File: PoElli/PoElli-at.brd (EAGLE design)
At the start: 85 x 56 mm, 146 parts, among them J3 M022.54MM, J4 M022.54MM, Q1 SI1307DL, Q2 FDV301N, Q3 FDMC2674, Q4 IRFL4310, SW1 A6H2101, T1 Coilcraft 230NL, T2 FLYBACK750311689, U2 NCP1117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

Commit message: routing draft v0.2, planes & routes in, optimization to be done..
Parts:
- moved C18 37.4 mm to (39.9, 47.0)
- moved C17 36.2 mm to (39.9, 48.0)
- moved TP8 35.5 mm to (2.00, 42.5)
- moved C43 27.6 mm to (37.4, 58.6)
- moved R14 25.1 mm to (22.9, 50.5)
- moved C4 24.4 mm to (12.2, 33.3), turned to 180 degrees
- moved C5 23.6 mm to (11.0, 34.7), turned to 270 degrees
- moved C44 23.3 mm to (37.4, 56.3)
- moved C6 21.1 mm to (10.9, 37.9), turned to 90 degrees
- moved D5 16.3 mm to (33.8, 50.3), turned to 90 degrees
- moved C45 15.7 mm to (37.4, 51.7)
- moved C46 15.0 mm to (37.4, 54.0)
- moved D18 14.0 mm to (36.7, 23.8), turned to 180 degrees
- moved R24 13.5 mm to (47.7, 35.6), turned to 270 degrees
- moved TP7 12.7 mm to (30.7, 40.5)
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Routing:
- net N$9: track 0.00 -> 82.3 mm, vias 0 -> 5
- net 5V: track 0.00 -> 70.9 mm, vias 0 -> 12
- net +3V3: track 0.00 -> 67.3 mm, vias 0 -> 8
- net N$11: track 0.00 -> 66.1 mm, vias 0 -> 2
- net N$12: track 0.00 -> 65.8 mm, vias 0 -> 2
- net N$13: track 0.00 -> 62.7 mm, vias 0 -> 2
- net N$14: track 0.00 -> 60.7 mm, vias 0 -> 2
- net ETH_SCK: track 0.00 -> 56.6 mm, vias 0 -> 2
- net ETH_MUX: track 0.00 -> 52.9 mm, vias 0 -> 4
- net POE_B+: track 0.00 -> 52.9 mm
- net N$21: track 0.00 -> 52.1 mm
- net SS2: track 0.00 -> 49.1 mm, vias 0 -> 2
- net ETH_MISO: track 0.00 -> 44.7 mm, vias 0 -> 2
- net ETH_MOSI: track 0.00 -> 42.4 mm, vias 0 -> 1
- net U4_INTVCC: track 0.00 -> 40.8 mm, vias 0 -> 4
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- added copper zone on layer 15, net +3V3
- added copper zone on layer 15, net 5V
- added copper zone on layer 15, net ENC-3V3
- added copper zone on layer 1, net GNDA
- added copper zone on layer 2, net GNDA
- added copper zone on layer 1, net RTN
- added copper zone on layer 2, net RTN
- added copper zone on layer 15, net VDD

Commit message: gnd vias, planes etc
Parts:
- moved U$2 95.4 mm to (94.7, 11.7)
- moved C41 2.75 mm to (35.3, 21.0)
- moved FB4 1.63 mm to (38.7, 18.1), turned to 90 degrees
- moved C25 1.56 mm to (63.6, 27.5), turned to 180 degrees
- moved R29 0.80 mm to (44.0, 13.2)
- moved R19 0.30 mm to (67.1, 26.8)
- moved C1 0.28 mm to (18.5, 34.2)
- moved D3 0.22 mm to (51.4, 37.9)
- moved R23 0.14 mm to (40.9, 14.4)
- moved R32 0.10 mm to (51.0, 35.5)
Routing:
- net N$76: track 13.3 -> 11.3 mm
- net POE_A-: track 30.6 -> 29.0 mm
- net ETH_MOSI: track 42.4 -> 43.6 mm
- net SS2: track 49.1 -> 50.2 mm
- net N$6: track 30.1 -> 31.1 mm
- net VSS: track 25.7 -> 26.6 mm
- net N$51: track 4.71 -> 5.53 mm
- net N$5: track 14.1 -> 13.3 mm
- net N$19: track 3.78 -> 4.57 mm
- net GNDA: vias 48 -> 139
- added copper zone on layer 16, net GNDA
- added copper zone on layer 16, net RTN

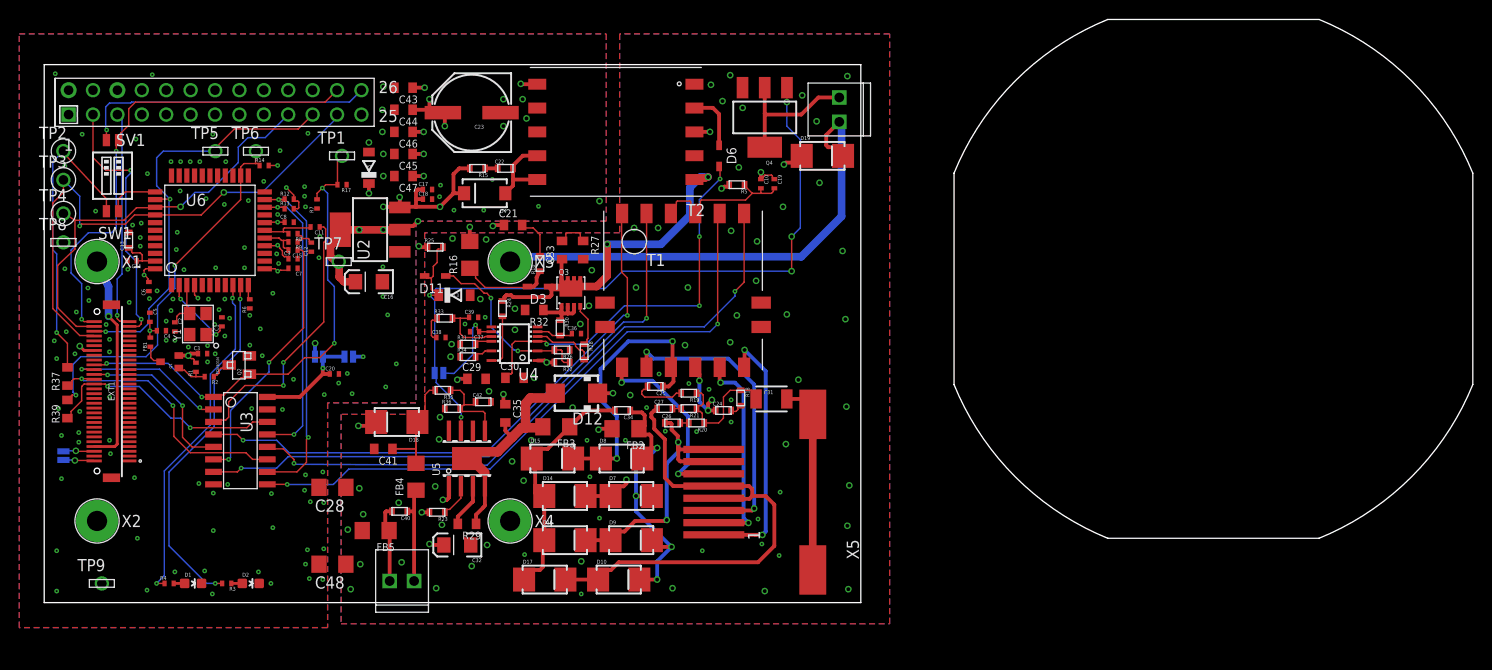
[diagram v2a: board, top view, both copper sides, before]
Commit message: smallest via drill to 0.25mm (was 0.2), + small improvments
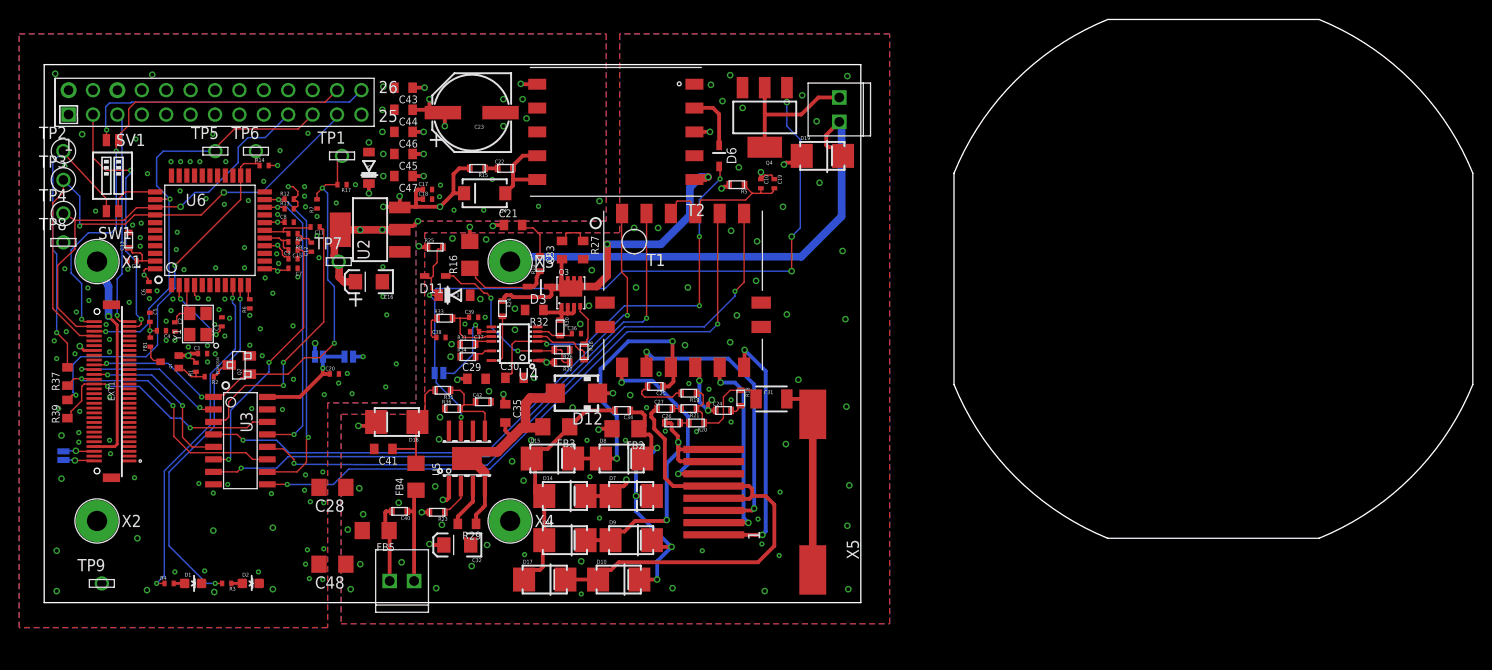
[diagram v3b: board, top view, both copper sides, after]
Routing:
- net +3V3: track 67.1 -> 66.6 mm
- net GNDA: vias 139 -> 145
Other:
- board text added: "+"

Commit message: review changes applied
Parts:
- removed U$2: (no value), ELL-i-Boards:DIN49073-1:2010-02-OUTLINE
- added C49, C50: 10nF, ELL-i-Passives:C0402
- added U$3: (no value), hapines:EH-LOGO
- C21: value 100nF -> 100nF 100V
- moved C19 21.6 mm to (54.7, 45.0), turned to 0 degrees
- moved R5 20.9 mm to (51.4, 45.8)
- moved C10 20.0 mm to (54.7, 46.5), turned to 0 degrees
- moved R10 6.57 mm to (46.1, 43.9), turned to 0 degrees
- moved D3 6.51 mm to (45.2, 39.9), turned to 90 degrees
- moved R16 2.77 mm to (42.2, 43.0), turned to 180 degrees
- moved C25 1.95 mm to (61.6, 27.5)
- moved T1 1.95 mm to (64.5, 37.5)
- moved R25 1.72 mm to (39.3, 41.0), turned to 270 degrees
- moved C36 1.60 mm to (53.8, 32.9)
- moved D13 1.57 mm to (41.3, 36.3)
- moved R24 1.40 mm to (46.3, 35.5)
- moved C39 1.40 mm to (43.3, 34.7)
- moved R30 1.40 mm to (52.3, 33.6)
- moved R33 1.40 mm to (40.3, 34.6)
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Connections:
- net GNDA: now also C49.1, C50.1
- net N$40: now also C49.2, C50.2
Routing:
- net +3V3: track 66.6 -> 46.4 mm, vias 8 -> 7
- net N$40: track 16.4 -> 32.9 mm, vias 0 -> 2
- net GNDA: track 22.9 -> 13.9 mm, vias 145 -> 147
- net N$9: track 82.3 -> 77.8 mm
- net N$33: track 9.57 -> 5.74 mm
- net N$34: track 4.46 -> 1.35 mm
- net N$28: track 39.2 -> 41.8 mm
- net POE_A-: track 29.0 -> 26.9 mm
- net N$12: track 65.8 -> 63.8 mm
- net N$11: track 66.1 -> 64.1 mm
- net POE_A+: track 27.7 -> 25.9 mm, vias 4 -> 3
- net N$17: track 19.1 -> 17.6 mm
- net N$21: track 52.1 -> 53.5 mm
- net N$2: track 27.2 -> 28.4 mm
- net N$76: track 11.3 -> 12.5 mm
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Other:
- outline, holes or cut-outs redrawn
- board text added: ""PoElli-at" PoE shield proto"
- board text added: "ELL-i.org"
- board text added: "https://github.com/Ell-i/ELL-i-Eagle-Boards"

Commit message: final tweakings, draft v0.9
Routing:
- net 5V: track 70.1 -> 61.5 mm, vias 12 -> 13
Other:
- outline, holes or cut-outs redrawn

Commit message: v1.0
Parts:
- moved R10 0.30 mm to (46.1, 43.6)
- moved C21 0.20 mm to (49.1, 43.8)
- moved D3 0.20 mm to (45.0, 39.9)
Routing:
- net N$12: track 63.8 -> 64.6 mm
- net GNDA: track 13.9 -> 13.8 mm, vias 147 -> 149
- added copper zone on layer 1, net N$30
- added copper zone on layer 15, net N$30
- added copper zone on layer 16, net N$30
- added copper zone on layer 2, net N$30
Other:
- board text added: "1"
- board text added: "2"
- board text added: "3"
- board text added: "4"
